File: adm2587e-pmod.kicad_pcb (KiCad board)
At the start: 2 copper layers, 49.5 x 20.3 mm, 20 parts, among them J1 PMOD, J2 OUT, J3 OUT, U1 ADM2587E

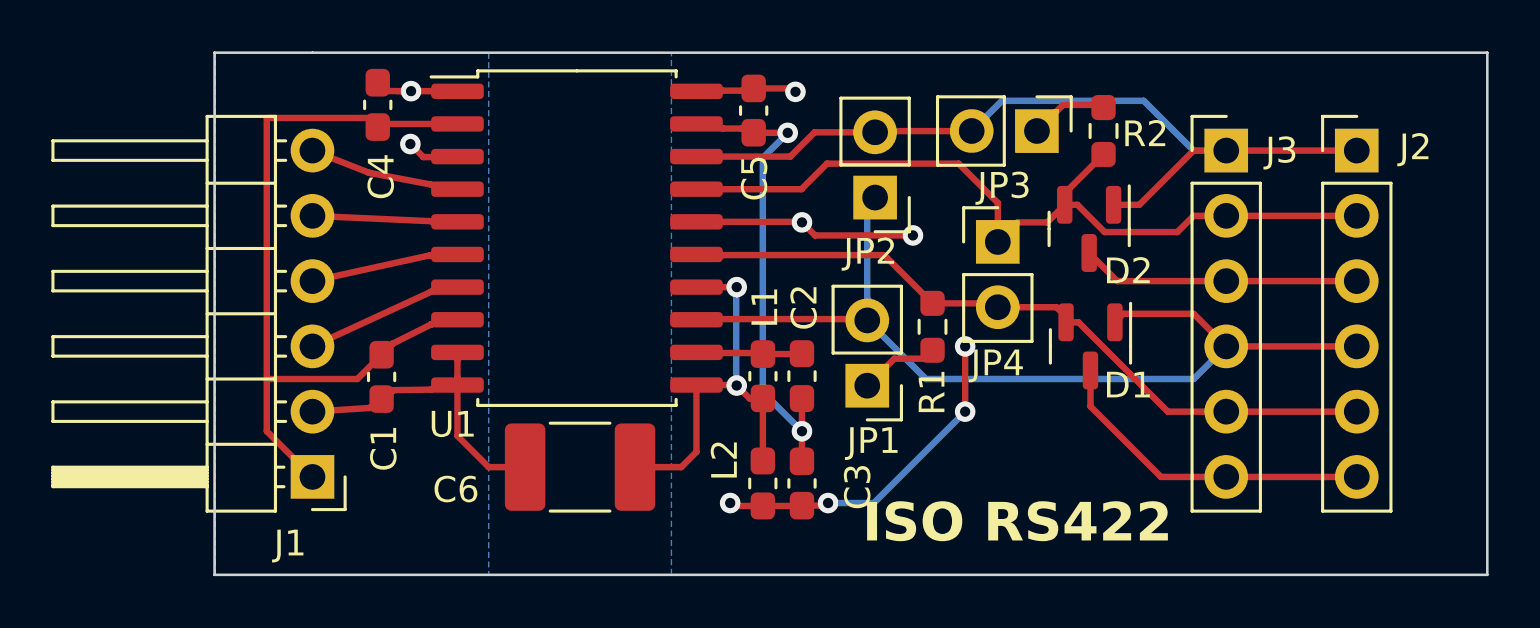
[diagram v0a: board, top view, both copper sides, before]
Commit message: clear the GND1 plane under filter
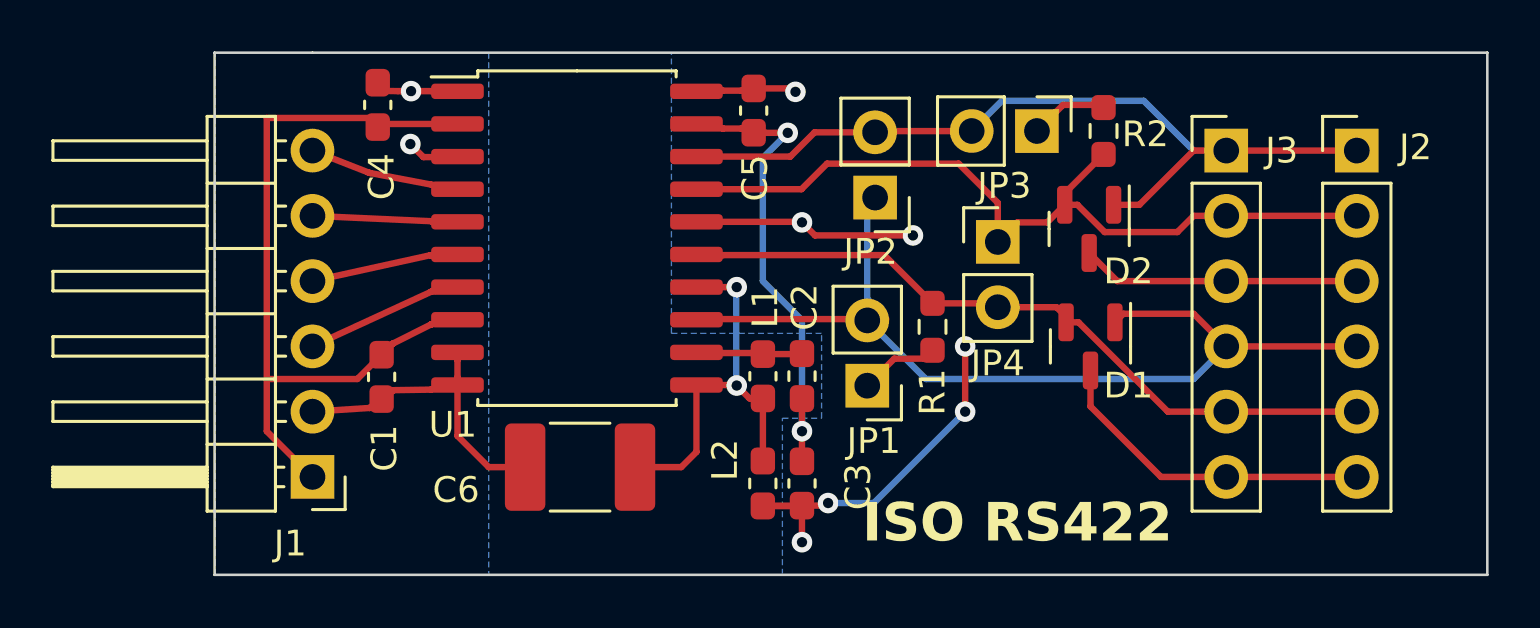
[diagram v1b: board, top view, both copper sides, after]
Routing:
- net GND1: track 49.6 -> 51.2 mm
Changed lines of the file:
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@@
   (via (at 113.03 66.802) (size 0.8) (drill 0.4) (layers "F.Cu" "B.Cu") (net 5))
   (via (at 112.4751 55.1895) (size 0.8) (drill 0.4) (layers "F.Cu" "B.Cu") (net 5))
-  (segment (start 111.506 56.1586) (end 111.506 65.278) (width 0.25) (layer "B.Cu") (net 5))
-  (segment (start 111.506 65.278) (end 113.03 66.802) (width 0.25) (layer "B.Cu") (net 5))
   (segment (start 112.4751 55.1895) (end 111.506 56.1586) (width 0.25) (layer "B.Cu") (net 5))
+  (segment (start 113.03 62.484) (end 113.03 66.802) (width 0.25) (layer "B.Cu") (net 5))
+  (segment (start 111.506 56.1586) (end 111.506 60.96) (width 0.25) (layer "B.Cu") (net 5))
+  (segment (start 111.506 60.96) (end 113.03 62.484) (width 0.25) (layer "B.Cu") (net 5))
   (segment (start 125.3005 60.96) (end 134.62 60.96) (width 0.25) (layer "F.Cu") (net 6))
   (segment (start 113.0175 69.709) (end 113.03 69.6965) (width 0.25) (layer "F.Cu") (net 6))
@@
   (segment (start 111.506 69.709) (end 113.0175 69.709) (width 0.25) (layer "F.Cu") (net 6))
   (segment (start 109.8234 53.5482) (end 109.9484 53.5482) (width 0.25) (layer "F.Cu") (net 6))
+  (segment (start 113.03 71.12) (end 113.03 69.709) (width 0.25) (layer "F.Cu") (net 6))
   (segment (start 127 68.58) (end 134.62 68.58) (width 0.25) (layer "F.Cu") (net 6))
   (segment (start 117.348 59.182) (end 113.538 59.182) (width 0.25) (layer "F.Cu") (net 6))
@@
   (segment (start 110.7982 53.5482) (end 111.1491 53.4615) (width 0.25) (layer "F.Cu") (net 6))
   (segment (start 119.38 66.04) (end 119.38 63.5) (width 0.25) (layer "F.Cu") (net 6))
+  (segment (start 113.03 69.709) (end 111.506 69.709) (width 0.25) (layer "F.Cu") (net 6))
   (segment (start 109.9484 53.5482) (end 110.6732 53.5482) (width 0.25) (layer "F.Cu") (net 6))
   (segment (start 108.9228 53.5732) (end 109.8234 53.5482) (width 0.25) (layer "F.Cu") (net 6))
-  (segment (start 111.506 69.709) (end 110.349 69.709) (width 0.25) (layer "F.Cu") (net 6))
   (segment (start 113.9455 69.6965) (end 114.046 69.596) (width 0.25) (layer "F.Cu") (net 6))
   (segment (start 110.6732 53.5482) (end 110.7982 53.5482) (width 0.25) (layer "F.Cu") (net 6))
   (segment (start 124.206 59.8655) (end 125.3005 60.96) (width 0.25) (layer "F.Cu") (net 6))
-  (segment (start 110.349 69.709) (end 110.236 69.596) (width 0.25) (layer "F.Cu") (net 6))
   (segment (start 124.2568 64.4375) (end 124.2568 65.8368) (width 0.25) (layer "F.Cu") (net 6))
   (segment (start 124.2568 65.8368) (end 127 68.58) (width 0.25) (layer "F.Cu") (net 6))
-  (via (at 110.236 69.596) (size 0.8) (drill 0.4) (layers "F.Cu" "B.Cu") (net 6))
+  (via (at 113.03 71.12) (size 0.8) (drill 0.4) (layers "F.Cu" "B.Cu") (net 6))
   (via (at 112.776 53.594) (size 0.8) (drill 0.4) (layers "F.Cu" "B.Cu") (net 6))
   (via (at 119.38 63.5) (size 0.8) (drill 0.4) (layers "F.Cu" "B.Cu") (net 6))
@@
       (pts
         (xy 139.7 72.39)
-        (xy 107.95 72.39)
+        (xy 112.268 72.39)
+        (xy 112.268 66.294)
+        (xy 113.792 66.294)
+        (xy 113.792 62.992)
+        (xy 107.95 62.992)
         (xy 107.95 52.07)
         (xy 139.7 52.07)

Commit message: more polish
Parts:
- moved C1 1.10 mm to (97.5, 64.0)
- moved C3 1.02 mm to (112.5, 67.9)
- moved L2 1.02 mm to (111.0, 67.9)
- moved C4 1.02 mm to (97.5, 54.2)
- moved C2 0.51 mm to (111.0, 64.6)
- moved L1 0.51 mm to (112.5, 64.6)
- moved C5 0.15 mm to (111.0, 54.3)
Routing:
- net GND: track 17.0 -> 20.6 mm
- net Net-(D1-A2): track 28.3 -> 29.6 mm
- net Net-(U1-Visoin): track 18.7 -> 17.7 mm
- net /VCC: track 30.1 -> 30.7 mm
- net GND1: track 51.2 -> 51.8 mm, vias 7 -> 9
- net Net-(U1-Visoout): track 4.12 -> 3.61 mm
